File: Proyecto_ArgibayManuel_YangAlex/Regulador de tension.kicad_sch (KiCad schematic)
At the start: 11 parts, among them IC1 LM1117

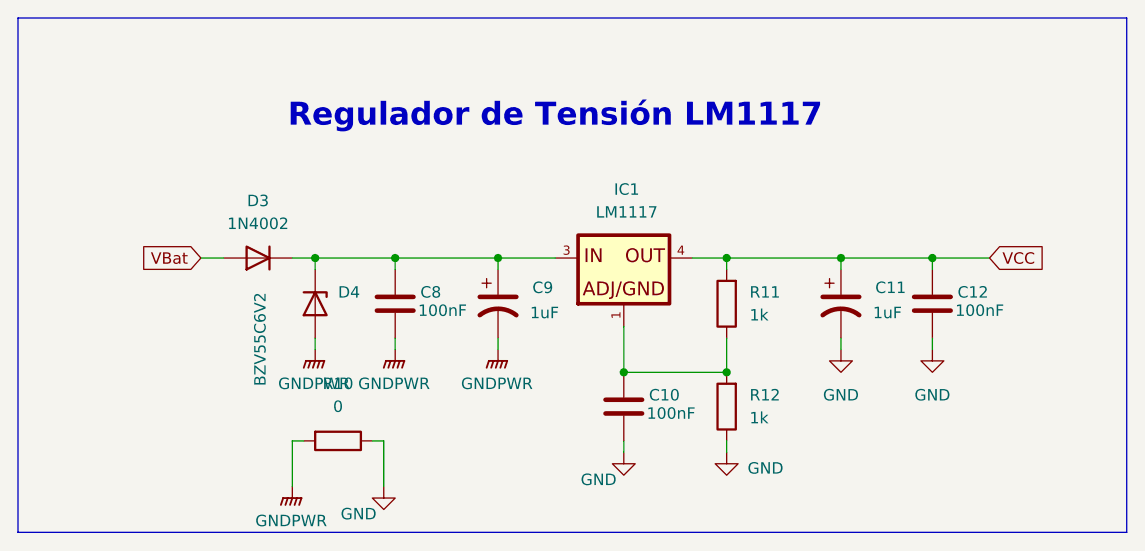
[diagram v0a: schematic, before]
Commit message: Separacion de Botonera
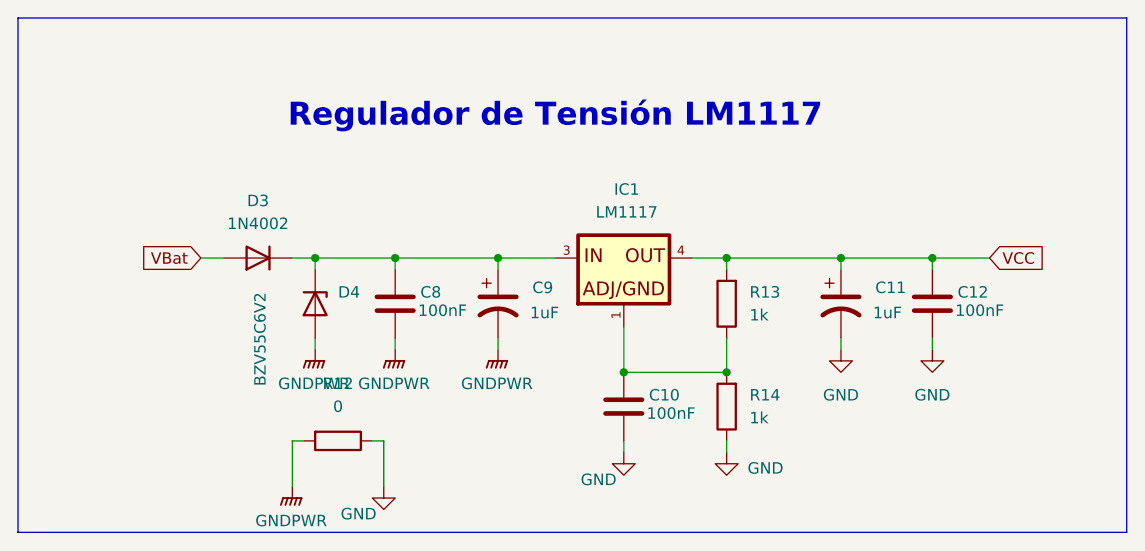
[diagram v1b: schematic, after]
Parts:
- renumbered R10 to R12, R11 to R13, R12 to R14
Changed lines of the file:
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@@
 		(on_board yes)
 		(dnp no)
-		(property "Reference" "#PWR028"
+		(property "Reference" "#PWR030"
 			(at 135.89 106.68 0)
 			(effects
@@
 			(project "Proyecto_ArgibayManuel_YangAlex"
 				(path "/b2dde924-33f5-41ab-a1bf-811873450a89/586cebd2-39d7-435a-989d-0b17f5522a13"
-					(reference "#PWR028")
+					(reference "#PWR030")
 					(unit 1)
 				)
@@
 		(dnp no)
 		(fields_autoplaced yes)
-		(property "Reference" "#PWR027"
+		(property "Reference" "#PWR031"
 			(at 137.16 90.17 0)
 			(effects
@@
 			(project "Proyecto_ArgibayManuel_YangAlex"
 				(path "/b2dde924-33f5-41ab-a1bf-811873450a89/586cebd2-39d7-435a-989d-0b17f5522a13"
-					(reference "#PWR027")
+					(reference "#PWR031")
 					(unit 1)
 				)
@@
 		(dnp no)
 		(fields_autoplaced yes)
-		(property "Reference" "#PWR032"
+		(property "Reference" "#PWR035"
 			(at 186.69 91.44 0)
 			(effects
@@
 			(project "Proyecto_ArgibayManuel_YangAlex"
 				(path "/b2dde924-33f5-41ab-a1bf-811873450a89/586cebd2-39d7-435a-989d-0b17f5522a13"
-					(reference "#PWR032")
+					(reference "#PWR035")
 					(unit 1)
 				)
@@
 		(on_board yes)
 		(dnp no)
-		(property "Reference" "#PWR031"
+		(property "Reference" "#PWR034"
 			(at 173.99 102.87 0)
 			(effects
@@
 			(project "Proyecto_ArgibayManuel_YangAlex"
 				(path "/b2dde924-33f5-41ab-a1bf-811873450a89/586cebd2-39d7-435a-989d-0b17f5522a13"
-					(reference "#PWR031")
+					(reference "#PWR034")
 					(unit 1)
 				)
@@
 		(dnp no)
 		(fields_autoplaced yes)
-		(property "Reference" "R10"
+		(property "Reference" "R12"
 			(at 130.81 88.9 90)
 			(effects
@@
 			(project "Proyecto_ArgibayManuel_YangAlex"
 				(path "/b2dde924-33f5-41ab-a1bf-811873450a89/586cebd2-39d7-435a-989d-0b17f5522a13"
-					(reference "R10")
+					(reference "R12")
 					(unit 1)
 				)
@@
 		(dnp no)
 		(fields_autoplaced yes)
-		(property "Reference" "#PWR026"
+		(property "Reference" "#PWR029"
 			(at 128.27 90.17 0)
 			(effects
@@
 			(project "Proyecto_ArgibayManuel_YangAlex"
 				(path "/b2dde924-33f5-41ab-a1bf-811873450a89/586cebd2-39d7-435a-989d-0b17f5522a13"
-					(reference "#PWR026")
+					(reference "#PWR029")
 					(unit 1)
 				)
@@
 		(dnp no)
 		(fields_autoplaced yes)
-		(property "Reference" "#PWR033"
+		(property "Reference" "#PWR036"
 			(at 196.85 91.44 0)
 			(effects
@@
 			(project "Proyecto_ArgibayManuel_YangAlex"
 				(path "/b2dde924-33f5-41ab-a1bf-811873450a89/586cebd2-39d7-435a-989d-0b17f5522a13"
-					(reference "#PWR033")
+					(reference "#PWR036")
 					(unit 1)
 				)
@@
 		(dnp no)
 		(fields_autoplaced yes)
-		(property "Reference" "R11"
+		(property "Reference" "R13"
 			(at 176.53 78.7399 0)
 			(effects
@@
 			(project "Proyecto_ArgibayManuel_YangAlex"
 				(path "/b2dde924-33f5-41ab-a1bf-811873450a89/586cebd2-39d7-435a-989d-0b17f5522a13"
-					(reference "R11")
+					(reference "R13")
 					(unit 1)
 				)
@@
 		(dnp no)
 		(fields_autoplaced yes)
-		(property "Reference" "#PWR029"
+		(property "Reference" "#PWR032"
 			(at 148.59 90.17 0)
 			(effects
@@
 			(project "Proyecto_ArgibayManuel_YangAlex"
 				(path "/b2dde924-33f5-41ab-a1bf-811873450a89/586cebd2-39d7-435a-989d-0b17f5522a13"
-					(reference "#PWR029")
+					(reference "#PWR032")
 					(unit 1)
 				)
@@
 		(dnp no)
 		(fields_autoplaced yes)
-		(property "Reference" "R12"
+		(property "Reference" "R14"
 			(at 176.53 90.1699 0)
 			(effects
@@
 			(project "Proyecto_ArgibayManuel_YangAlex"
 				(path "/b2dde924-33f5-41ab-a1bf-811873450a89/586cebd2-39d7-435a-989d-0b17f5522a13"
-					(reference "R12")
+					(reference "R14")
 					(unit 1)
 				)
@@
 		(dnp no)
 		(fields_autoplaced yes)
-		(property "Reference" "#PWR025"
+		(property "Reference" "#PWR028"
 			(at 125.73 105.41 0)
 			(effects
@@
 			(project "Proyecto_ArgibayManuel_YangAlex"
 				(path "/b2dde924-33f5-41ab-a1bf-811873450a89/586cebd2-39d7-435a-989d-0b17f5522a13"
-					(reference "#PWR025")
+					(reference "#PWR028")
 					(unit 1)
 				)
@@
 		(on_board yes)
 		(dnp no)
-		(property "Reference" "#PWR030"
+		(property "Reference" "#PWR033"
 			(at 162.56 102.87 0)
 			(effects
@@
 			(project "Proyecto_ArgibayManuel_YangAlex"
 				(path "/b2dde924-33f5-41ab-a1bf-811873450a89/586cebd2-39d7-435a-989d-0b17f5522a13"
-					(reference "#PWR030")
-					(unit 1)
-				)
+					(reference "#PWR033")
+					(unit 1)
+				)

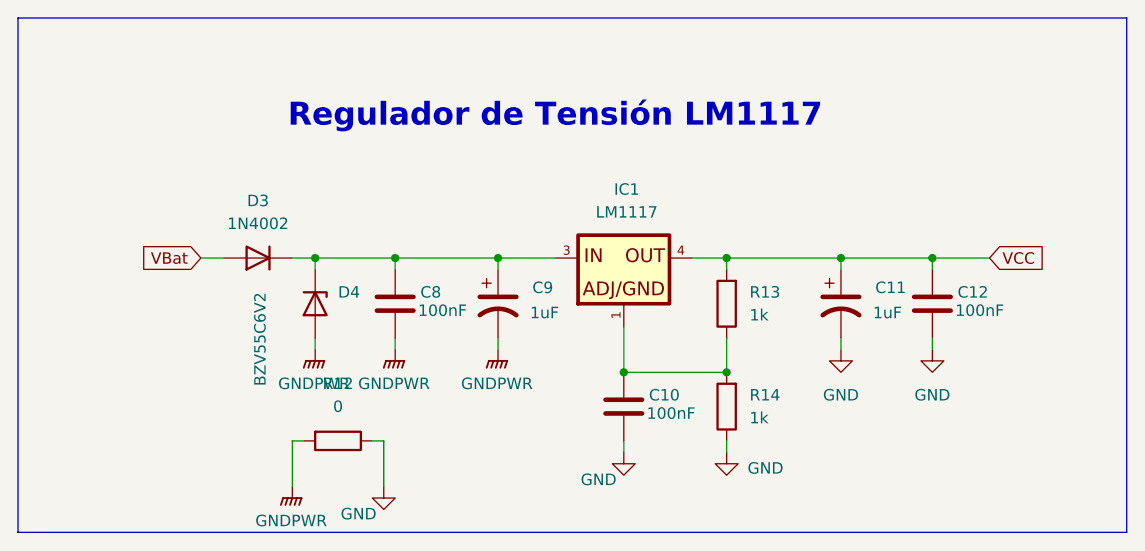
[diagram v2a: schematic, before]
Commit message: Cambio del sensor
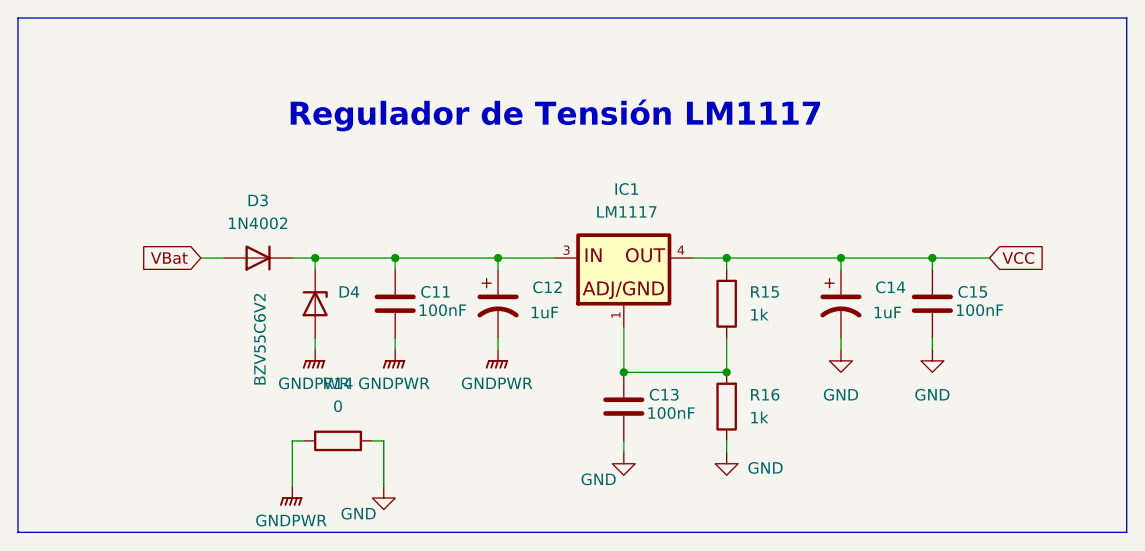
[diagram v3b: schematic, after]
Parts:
- renumbered C8 to C11, C9 to C12, C10 to C13, C11 to C14, C12 to C15, R12 to R14, R13 to R15, R14 to R16
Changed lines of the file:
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@@
 		(on_board yes)
 		(dnp no)
-		(property "Reference" "#PWR033"
+		(property "Reference" "#PWR038"
 			(at 135.89 106.68 0)
 			(effects
@@
 			(project "Proyecto_ArgibayManuel_YangAlex"
 				(path "/b2dde924-33f5-41ab-a1bf-811873450a89/586cebd2-39d7-435a-989d-0b17f5522a13"
-					(reference "#PWR033")
+					(reference "#PWR038")
 					(unit 1)
 				)
@@
 		(dnp no)
 		(fields_autoplaced yes)
-		(property "Reference" "#PWR034"
+		(property "Reference" "#PWR039"
 			(at 137.16 90.17 0)
 			(effects
@@
 			(project "Proyecto_ArgibayManuel_YangAlex"
 				(path "/b2dde924-33f5-41ab-a1bf-811873450a89/586cebd2-39d7-435a-989d-0b17f5522a13"
-					(reference "#PWR034")
+					(reference "#PWR039")
 					(unit 1)
 				)
@@
 		(dnp no)
 		(fields_autoplaced yes)
-		(property "Reference" "#PWR038"
+		(property "Reference" "#PWR043"
 			(at 186.69 91.44 0)
 			(effects
@@
 			(project "Proyecto_ArgibayManuel_YangAlex"
 				(path "/b2dde924-33f5-41ab-a1bf-811873450a89/586cebd2-39d7-435a-989d-0b17f5522a13"
-					(reference "#PWR038")
+					(reference "#PWR043")
 					(unit 1)
 				)
@@
 		(on_board yes)
 		(dnp no)
-		(property "Reference" "C8"
+		(property "Reference" "C11"
 			(at 139.954 78.74 0)
 			(effects
@@
 			(project "Proyecto_ArgibayManuel_YangAlex"
 				(path "/b2dde924-33f5-41ab-a1bf-811873450a89/586cebd2-39d7-435a-989d-0b17f5522a13"
-					(reference "C8")
+					(reference "C11")
 					(unit 1)
 				)
@@
 		(on_board yes)
 		(dnp no)
-		(property "Reference" "#PWR037"
+		(property "Reference" "#PWR042"
 			(at 173.99 102.87 0)
 			(effects
@@
 			(project "Proyecto_ArgibayManuel_YangAlex"
 				(path "/b2dde924-33f5-41ab-a1bf-811873450a89/586cebd2-39d7-435a-989d-0b17f5522a13"
-					(reference "#PWR037")
+					(reference "#PWR042")
 					(unit 1)
 				)
@@
 		(dnp no)
 		(fields_autoplaced yes)
-		(property "Reference" "R12"
+		(property "Reference" "R14"
 			(at 130.81 88.9 90)
 			(effects
@@
 			(project "Proyecto_ArgibayManuel_YangAlex"
 				(path "/b2dde924-33f5-41ab-a1bf-811873450a89/586cebd2-39d7-435a-989d-0b17f5522a13"
-					(reference "R12")
+					(reference "R14")
 					(unit 1)
 				)
@@
 		(on_board yes)
 		(dnp no)
-		(property "Reference" "C9"
+		(property "Reference" "C12"
 			(at 152.4 78.232 0)
 			(effects
@@
 			(project "Proyecto_ArgibayManuel_YangAlex"
 				(path "/b2dde924-33f5-41ab-a1bf-811873450a89/586cebd2-39d7-435a-989d-0b17f5522a13"
-					(reference "C9")
+					(reference "C12")
 					(unit 1)
 				)
@@
 		(dnp no)
 		(fields_autoplaced yes)
-		(property "Reference" "#PWR032"
+		(property "Reference" "#PWR037"
 			(at 128.27 90.17 0)
 			(effects
@@
 			(project "Proyecto_ArgibayManuel_YangAlex"
 				(path "/b2dde924-33f5-41ab-a1bf-811873450a89/586cebd2-39d7-435a-989d-0b17f5522a13"
-					(reference "#PWR032")
+					(reference "#PWR037")
 					(unit 1)
 				)
@@
 		(dnp no)
 		(fields_autoplaced yes)
-		(property "Reference" "#PWR039"
+		(property "Reference" "#PWR044"
 			(at 196.85 91.44 0)
 			(effects
@@
 			(project "Proyecto_ArgibayManuel_YangAlex"
 				(path "/b2dde924-33f5-41ab-a1bf-811873450a89/586cebd2-39d7-435a-989d-0b17f5522a13"
-					(reference "#PWR039")
+					(reference "#PWR044")
 					(unit 1)
 				)
@@
 		(dnp no)
 		(fields_autoplaced yes)
-		(property "Reference" "R13"
+		(property "Reference" "R15"
 			(at 176.53 78.7399 0)
 			(effects
@@
 			(project "Proyecto_ArgibayManuel_YangAlex"
 				(path "/b2dde924-33f5-41ab-a1bf-811873450a89/586cebd2-39d7-435a-989d-0b17f5522a13"
-					(reference "R13")
+					(reference "R15")
 					(unit 1)
 				)
@@
 		(dnp no)
 		(fields_autoplaced yes)
-		(property "Reference" "#PWR035"
+		(property "Reference" "#PWR040"
 			(at 148.59 90.17 0)
 			(effects
@@
 			(project "Proyecto_ArgibayManuel_YangAlex"
 				(path "/b2dde924-33f5-41ab-a1bf-811873450a89/586cebd2-39d7-435a-989d-0b17f5522a13"
-					(reference "#PWR035")
+					(reference "#PWR040")
 					(unit 1)
 				)
@@
 		(dnp no)
 		(fields_autoplaced yes)
-		(property "Reference" "R14"
+		(property "Reference" "R16"
 			(at 176.53 90.1699 0)
 			(effects
@@
 			(project "Proyecto_ArgibayManuel_YangAlex"
 				(path "/b2dde924-33f5-41ab-a1bf-811873450a89/586cebd2-39d7-435a-989d-0b17f5522a13"
-					(reference "R14")
+					(reference "R16")
 					(unit 1)
 				)
@@
 		(on_board yes)
 		(dnp no)
-		(property "Reference" "C10"
+		(property "Reference" "C13"
 			(at 165.354 90.17 0)
 			(effects
@@
 			(project "Proyecto_ArgibayManuel_YangAlex"
 				(path "/b2dde924-33f5-41ab-a1bf-811873450a89/586cebd2-39d7-435a-989d-0b17f5522a13"
-					(reference "C10")
+					(reference "C13")
 					(unit 1)
 				)
@@
 		(dnp no)
 		(fields_autoplaced yes)
-		(property "Reference" "#PWR031"
+		(property "Reference" "#PWR036"
 			(at 125.73 105.41 0)
 			(effects
@@
 			(project "Proyecto_ArgibayManuel_YangAlex"
 				(path "/b2dde924-33f5-41ab-a1bf-811873450a89/586cebd2-39d7-435a-989d-0b17f5522a13"
-					(reference "#PWR031")
+					(reference "#PWR036")
 					(unit 1)
 				)
@@
 		(on_board yes)
 		(dnp no)
-		(property "Reference" "#PWR036"
+		(property "Reference" "#PWR041"
 			(at 162.56 102.87 0)
 			(effects
@@
 			(project "Proyecto_ArgibayManuel_YangAlex"
 				(path "/b2dde924-33f5-41ab-a1bf-811873450a89/586cebd2-39d7-435a-989d-0b17f5522a13"
-					(reference "#PWR036")
+					(reference "#PWR041")
 					(unit 1)
 				)
@@
 		(on_board yes)
 		(dnp no)
-		(property "Reference" "C12"
+		(property "Reference" "C15"
 			(at 199.644 78.74 0)
 			(effects
@@
 			(project "Proyecto_ArgibayManuel_YangAlex"
 				(path "/b2dde924-33f5-41ab-a1bf-811873450a89/586cebd2-39d7-435a-989d-0b17f5522a13"
-					(reference "C12")
+					(reference "C15")
 					(unit 1)
 				)
@@
 		(on_board yes)
 		(dnp no)
-		(property "Reference" "C11"
+		(property "Reference" "C14"
 			(at 190.5 78.232 0)
 			(effects
@@
 			(project "Proyecto_ArgibayManuel_YangAlex"
 				(path "/b2dde924-33f5-41ab-a1bf-811873450a89/586cebd2-39d7-435a-989d-0b17f5522a13"
-					(reference "C11")
-					(unit 1)
-				)
+					(reference "C14")
+					(unit 1)
+				)
